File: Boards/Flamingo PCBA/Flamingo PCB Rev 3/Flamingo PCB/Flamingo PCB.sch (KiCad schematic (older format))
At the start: 0 parts

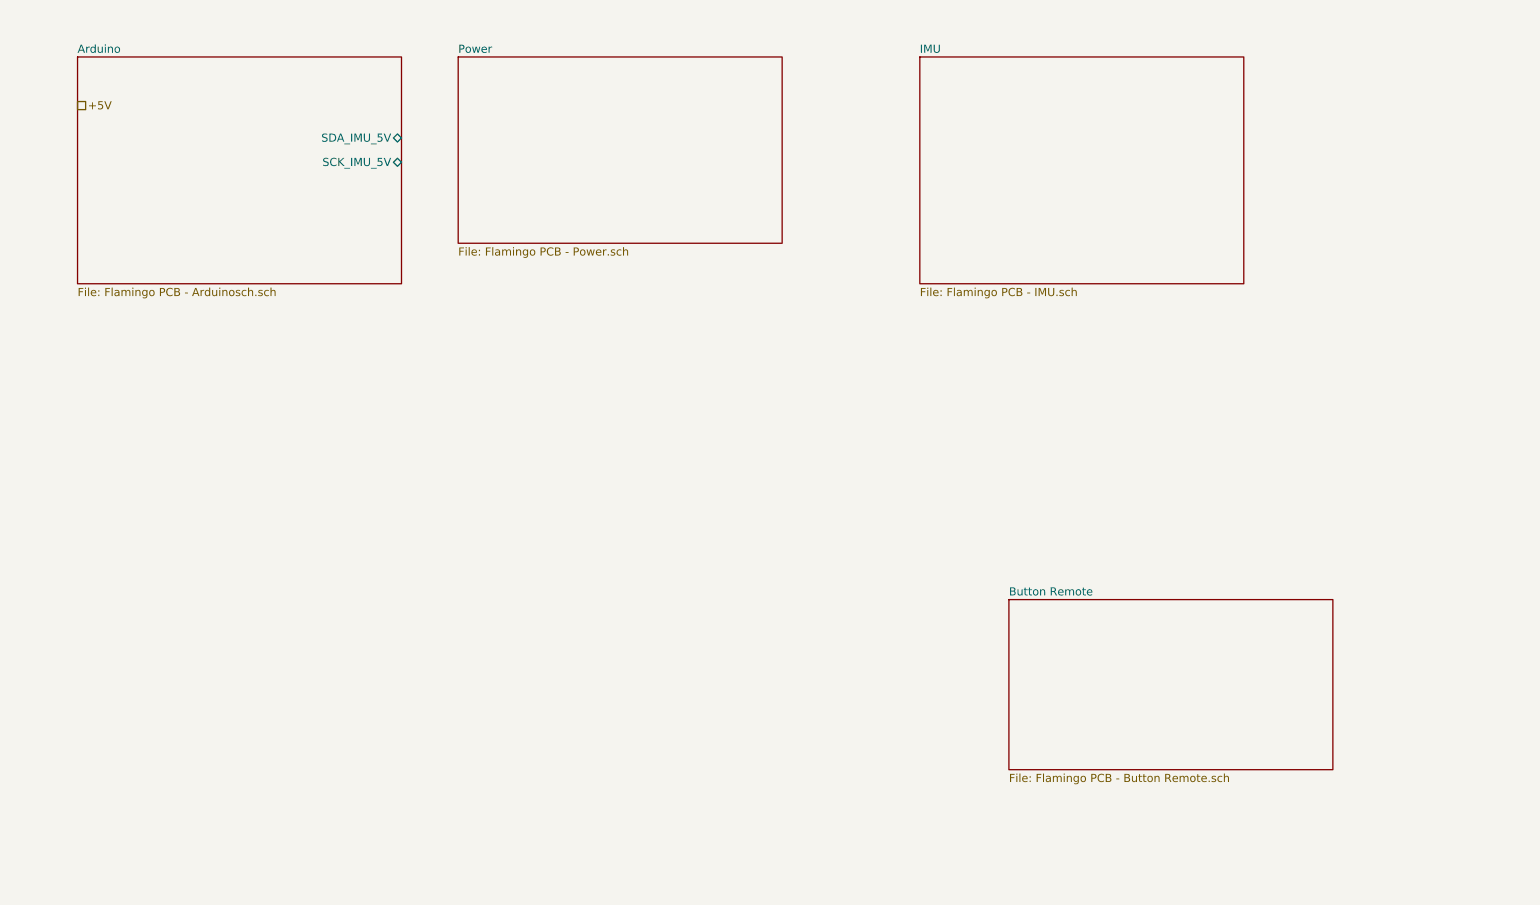
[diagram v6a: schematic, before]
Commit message: Wired up top-level sheet, fixed some hier. pins
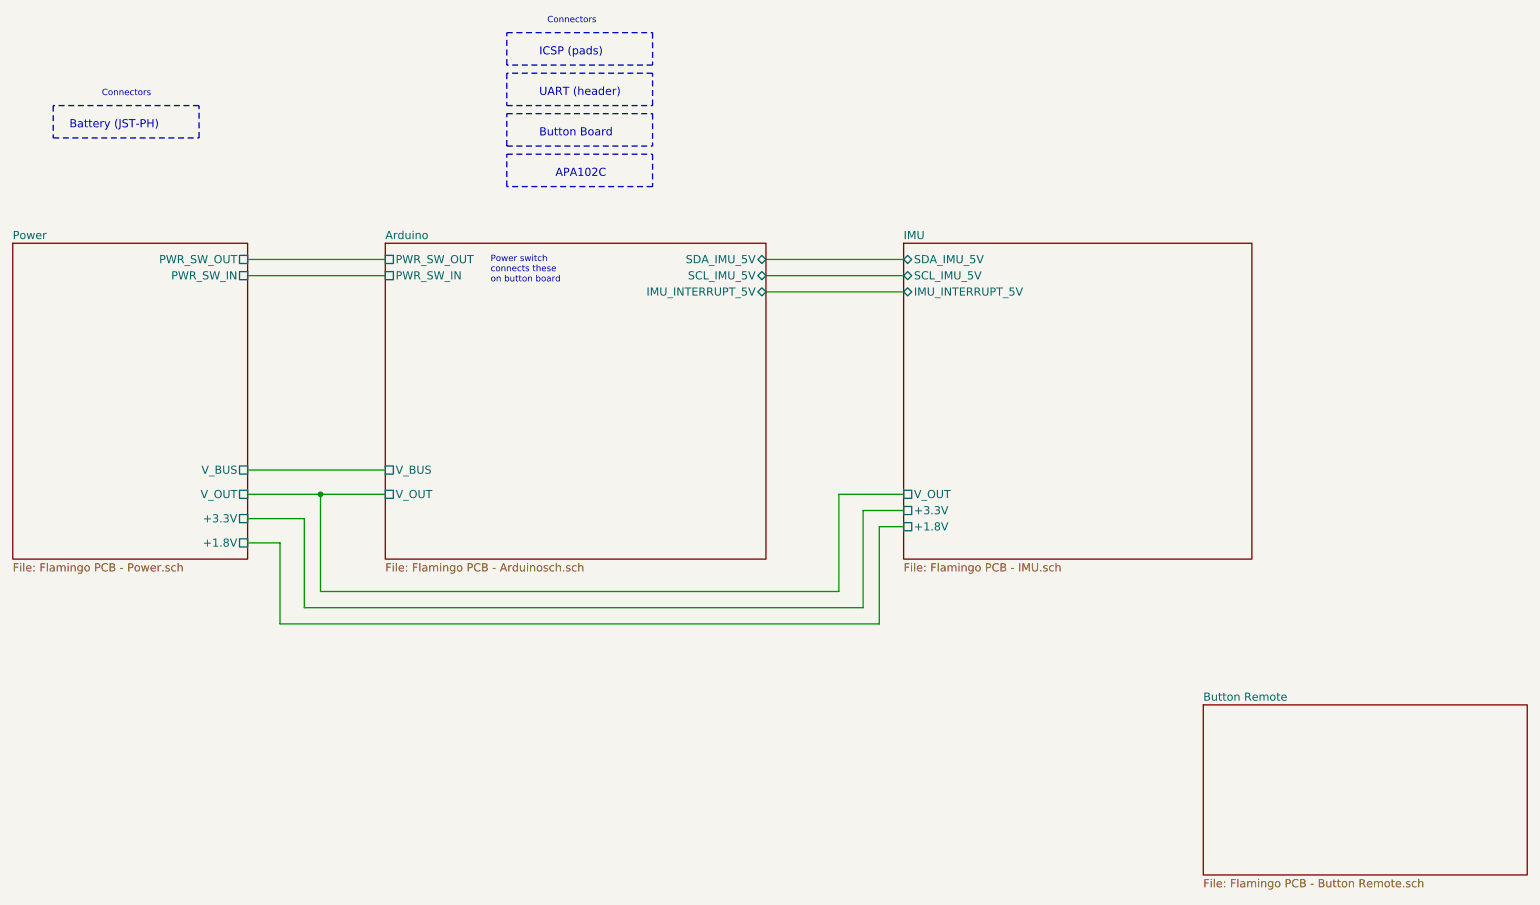
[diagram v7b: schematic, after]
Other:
- note added: "APA102C"
- note added: "Battery (JST-PH)"
- note added: "Button Board"
- note added: "Connectors"
- note added: "ICSP (pads)"
- note added: "Power switch\nconnects these\non button board"
- note added: "UART (header)"
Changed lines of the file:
@@
 $EndDescr
 $Sheet
-S 1300 1500 2000 1400
-U 5F780A01
-F0 "Arduino" 50
-F1 "Flamingo PCB - Arduinosch.sch" 50
-F2 "SDA_IMU_5V" B R 3300 2000 50
-F3 "SCK_IMU_5V" B R 3300 2150 50
-$EndSheet
-$Sheet
-S 6500 1500 2000 1400
-U 5F780E58
-F0 "IMU" 50
-F1 "Flamingo PCB - IMU.sch" 50
-$EndSheet
-$Sheet
-S 3650 1500 2000 1150
+S 900  2650 1450 1950
 U 5F780F7E
 F0 "Power" 50
 F1 "Flamingo PCB - Power.sch" 50
+F2 "+3.3V" U R 2350 4350 50
+F3 "+1.8V" U R 2350 4500 50
+F4 "V_OUT" U R 2350 4200 50
+F5 "V_BUS" U R 2350 4050 50
+F6 "PWR_SW_IN" U R 2350 2850 50
+F7 "PWR_SW_OUT" U R 2350 2750 50
 $EndSheet
-Text HLabel 1300 1800 2    50   UnSpc ~ 0
-+5V
+Wire Wire Line
+	2350 2750 3200 2750
+Wire Wire Line
+	2350 2850 3200 2850
 $Sheet
-S 7050 4850 2000 1050
+S 8250 5500 2000 1050
 U 5FA54816
 F0 "Button Remote" 50
 F1 "Flamingo PCB - Button Remote.sch" 50
 $EndSheet
+Text Notes 3850 2900 0    39   ~ 0
+Power switch\nconnects these\non button board
+$Sheet
+S 6400 2650 2150 1950
+U 5F780E58
+F0 "IMU" 50
+F1 "Flamingo PCB - IMU.sch" 50
+F2 "V_OUT" U L 6400 4200 50
+F3 "+3.3V" U L 6400 4300 50
+F4 "+1.8V" U L 6400 4400 50
+F5 "SDA_IMU_5V" B L 6400 2750 50
+F6 "SCL_IMU_5V" B L 6400 2850 50
+F7 "IMU_INTERRUPT_5V" B L 6400 2950 50
+$EndSheet
+$Sheet
+S 3200 2650 2350 1950
+U 5F780A01
+F0 "Arduino" 50
+F1 "Flamingo PCB - Arduinosch.sch" 50
+F2 "SDA_IMU_5V" B R 5550 2750 50
+F3 "V_BUS" U L 3200 4050 50
+F4 "V_OUT" U L 3200 4200 50
+F5 "IMU_INTERRUPT_5V" B R 5550 2950 50
+F6 "PWR_SW_IN" U L 3200 2850 50
+F7 "PWR_SW_OUT" U L 3200 2750 50
+F8 "SCL_IMU_5V" B R 5550 2850 50
+$EndSheet
+Wire Wire Line
+	5550 2950 6400 2950
+Wire Wire Line
+	6400 2850 5550 2850
+Wire Wire Line
+	5550 2750 6400 2750
+Wire Wire Line
+	2350 4200 2800 4200
+Wire Wire Line
+	2350 4500 2550 4500
+Wire Wire Line
+	2550 4500 2550 5000
+Wire Wire Line
+	2550 5000 6250 5000
+Wire Wire Line
+	6250 5000 6250 4400
+Wire Wire Line
+	6250 4400 6400 4400
+Wire Wire Line
+	2350 4350 2700 4350
+Wire Wire Line
+	2700 4350 2700 4900
+Wire Wire Line
+	2700 4900 6150 4900
+Wire Wire Line
+	6150 4900 6150 4300
+Wire Wire Line
+	6150 4300 6400 4300
+Wire Wire Line
+	2800 4200 2800 4800
+Wire Wire Line
+	2800 4800 6000 4800
+Wire Wire Line
+	6000 4800 6000 4200
+Wire Wire Line
+	6000 4200 6400 4200
+Connection ~ 2800 4200
+Wire Wire Line
+	2800 4200 3200 4200
+Wire Wire Line
+	2350 4050 3200 4050
+Wire Notes Line
+	3950 1550 3950 1350
+Wire Notes Line
+	4850 1350 4850 1550
+Text Notes 4150 1500 0    50   ~ 0
+ICSP (pads)
+Wire Notes Line
+	3950 1350 4850 1350
+Wire Notes Line
+	4850 1550 3950 1550
+Text Notes 4150 1750 0    50   ~ 0
+UART (header)
+Text Notes 4150 2000 0    50   ~ 0
+Button Board
+Wire Notes Line
+	3950 1600 3950 1800
+Wire Notes Line
+	3950 1800 4850 1800
+Wire Notes Line
+	4850 1800 4850 1600
+Wire Notes Line
+	4850 1600 3950 1600
+Wire Notes Line
+	3950 2050 4850 2050
+Wire Notes Line
+	3950 2050 3950 1850
+Wire Notes Line
+	3950 1850 4850 1850
+Wire Notes Line
+	4850 1850 4850 2050
+Text Notes 4200 1300 0    39   ~ 0
+Connectors
+Text Notes 1250 1950 0    50   ~ 0
+Battery (JST-PH)
+Text Notes 1450 1750 0    39   ~ 0
+Connectors
+Wire Notes Line
+	1150 2000 2050 2000
+Wire Notes Line
+	2050 2000 2050 1800
+Wire Notes Line
+	2050 1800 1150 1800
+Wire Notes Line
+	1150 1800 1150 2000
+Text Notes 4250 2250 0    50   ~ 0
+APA102C
+Wire Notes Line
+	3950 2100 4850 2100
+Wire Notes Line
+	4850 2100 4850 2300
+Wire Notes Line
+	4850 2300 3950 2300
+Wire Notes Line
+	3950 2300 3950 2100
 $EndSCHEMATC

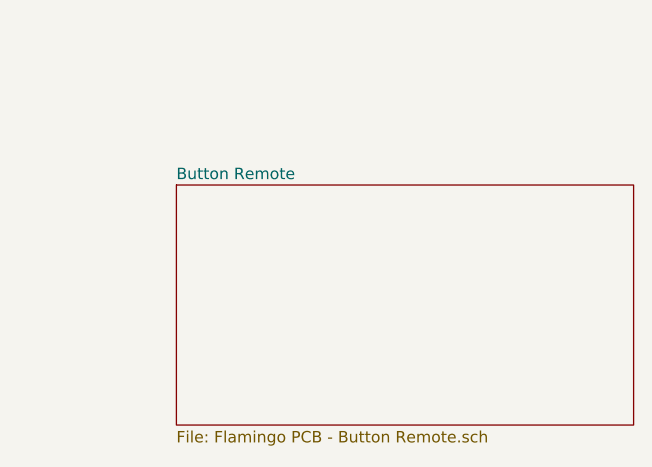
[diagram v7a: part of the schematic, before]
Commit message: Added Button Remote project
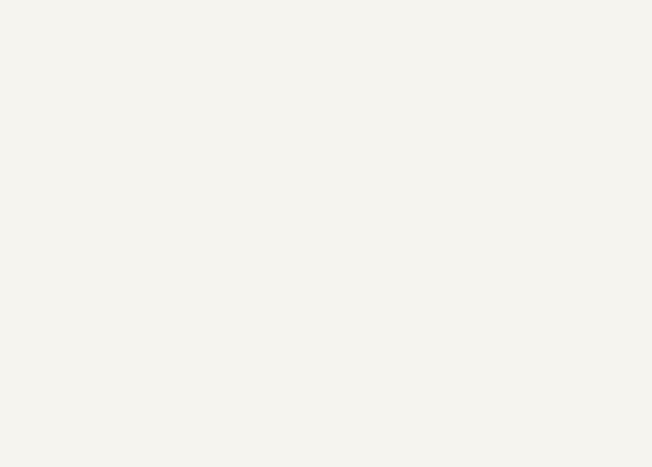
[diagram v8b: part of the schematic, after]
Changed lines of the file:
@@
 $Descr USLetter 11000 8500
 encoding utf-8
-Sheet 1 5
+Sheet 1 4
 Title "Flamingo PCB"
 Date "2020-09-29"
@@
 Wire Wire Line
 	2350 2850 3200 2850
-$Sheet
-S 8250 5500 2000 1050
-U 5FA54816
-F0 "Button Remote" 50
-F1 "Flamingo PCB - Button Remote.sch" 50
-$EndSheet
 Text Notes 3850 2900 0    39   ~ 0
 Power switch\nconnects these\non button board
